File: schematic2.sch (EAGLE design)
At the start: 76 parts, among them IC6 DS3231/SO

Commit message: Corrected unity gain buffer amplifiers for reference voltages into the instrumentation amps.
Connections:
- new net REF_BEAM: BEAM_Z.REF, REFC.-IN, REFC.OUT
- new net REF_JOYX: JOY_Y.REF, REFB.-IN, REFB.OUT
- new net REF_JOYY: JOY_X.REF, REFA.-IN, REFA.OUT
- net A3: now also REFA.+IN; no longer JOY_X.REF, REFA.-IN, REFA.OUT
- net A4: now also REFB.+IN; no longer JOY_Y.REF, REFB.-IN, REFB.OUT
- net A5: now also REFC.+IN; no longer BEAM_Z.REF, REFC.-IN, REFC.OUT
- net AGND: no longer REFA.+IN, REFB.+IN, REFC.+IN

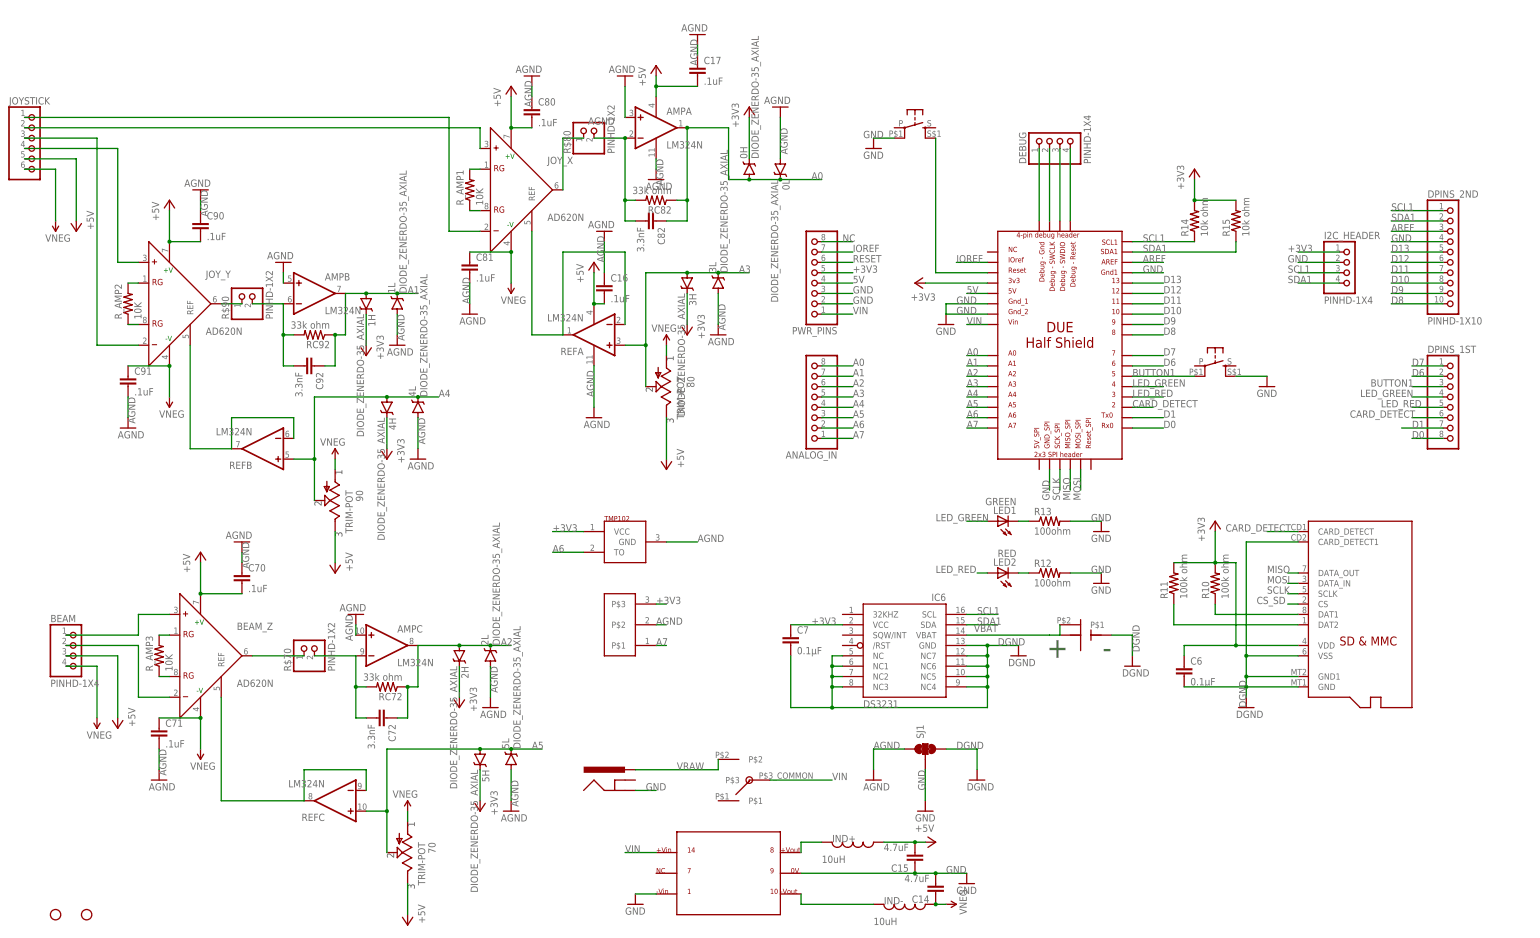
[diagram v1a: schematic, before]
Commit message: Moved the amps around again, wired most of the traces. Discovered that I never connected CS_SD, it is now wired to Due pin D10.
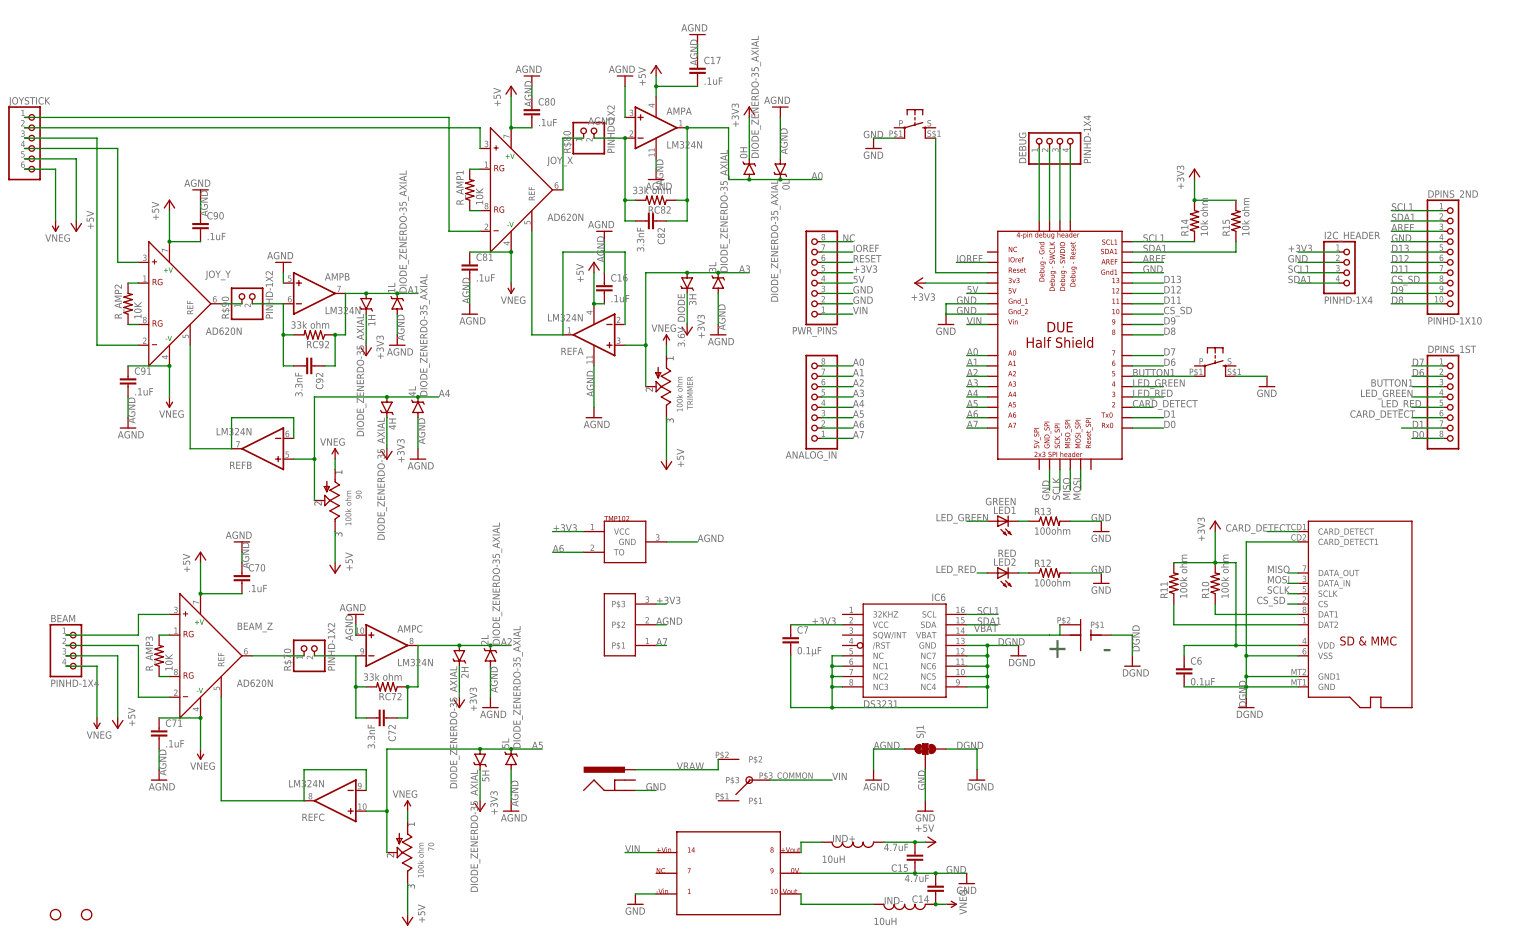
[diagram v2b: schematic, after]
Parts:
- removed 80: TRIM-POT, Felicia_force_logger:TRIM-POT
- added TRIMMER: 100k ohm, Felicia_force_logger:TRIMMER_POTENTIOMETER_TT_ELEC67W
- 3H: value DIODE_ZENERDO-35_AXIAL -> 3.6V_DIODE
- 70, 90: value TRIM-POT -> 100k ohm; device Felicia_force_logger:TRIM-POT -> miller:TRIMMER_POTENTIOMETER_TT_ELEC67W
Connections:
- removed net D10: DPINS_2ND.8, U$1.10
- net +5V: now also TRIMMER.P$3; no longer 80.P$3
- net A3: now also TRIMMER.P$2; no longer 80.P$2
- net CS_SD: now also DPINS_2ND.8, U$1.10
- net VNEG: now also TRIMMER.P$1; no longer 80.P$1
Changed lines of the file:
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@@
 <?xml version="1.0" encoding="utf-8"?>
 <!DOCTYPE eagle SYSTEM "eagle.dtd">
-<eagle version="7.0.0">
+<eagle version="7.2.0">
 <drawing>
 <settings>
@@
 <layer number="113" name="IDFDebug" color="4" fill="1" visible="yes" active="yes"/>
 <layer number="116" name="Patch_BOT" color="9" fill="4" visible="yes" active="yes"/>
+<layer number="118" name="Rect_Pads" color="7" fill="1" visible="no" active="no"/>
 <layer number="121" name="_tsilk" color="7" fill="1" visible="yes" active="yes"/>
 <layer number="122" name="_bsilk" color="7" fill="1" visible="yes" active="yes"/>
@@
 <layer number="223" name="223bmp" color="24" fill="1" visible="no" active="no"/>
 <layer number="224" name="224bmp" color="25" fill="1" visible="no" active="no"/>
+<layer number="231" name="Eagle3D_PG1" color="7" fill="1" visible="no" active="no"/>
+<layer number="232" name="Eagle3D_PG2" color="7" fill="1" visible="no" active="no"/>
+<layer number="233" name="Eagle3D_PG3" color="7" fill="1" visible="no" active="no"/>
 <layer number="248" name="Housing" color="7" fill="1" visible="yes" active="yes"/>
 <layer number="249" name="Edge" color="7" fill="1" visible="yes" active="yes"/>
@@
 <part name="BEAM_Z" library="Felicia_force_logger" deviceset="AD620" device="N"/>
 <part name="REF" library="Felicia_force_logger" deviceset="LM324" device="N"/>
-<part name="90" library="Felicia_force_logger" deviceset="TRIM-POT" device=""/>
-<part name="80" library="Felicia_force_logger" deviceset="TRIM-POT" device=""/>
-<part name="70" library="Felicia_force_logger" deviceset="TRIM-POT" device=""/>
+<part name="90" library="miller" deviceset="TRIMMER_POTENTIOMETER_TT_ELEC" device="67W" value="100k ohm"/>
+<part name="TRIMMER" library="Felicia_force_logger" deviceset="TRIMMER_POTENTIOMETER_TT_ELEC" device="67W" value="100k ohm"/>
+<part name="70" library="miller" deviceset="TRIMMER_POTENTIOMETER_TT_ELEC" device="67W" value="100k ohm"/>
 <part name="AMP" library="Felicia_force_logger" deviceset="LM324" device="N"/>
 <part name="GND4" library="Felicia_force_logger" deviceset="AGND" device=""/>
@@
 <part name="+3V4" library="supply1" deviceset="+3V3" device=""/>
 <part name="GND13" library="Felicia_force_logger" deviceset="AGND" device=""/>
-<part name="3H" library="Felicia_force_logger" deviceset="DIODE_ZENER" device="DO-35_AXIAL"/>
+<part name="3H" library="Felicia_force_logger" deviceset="DIODE_ZENER" device="DO-35_AXIAL" value="3.6V_DIODE"/>
 <part name="3L" library="Felicia_force_logger" deviceset="DIODE_ZENER" device="DO-35_AXIAL"/>
 <part name="+3V5" library="supply1" deviceset="+3V3" device=""/>
@@
 <instance part="REF" gate="C" x="73.66" y="33.02" rot="R180"/>
 <instance part="90" gate="G$1" x="73.66" y="106.68" rot="R270"/>
-<instance part="80" gate="G$1" x="154.94" y="134.62" rot="R270"/>
+<instance part="TRIMMER" gate="G$1" x="154.94" y="134.62" rot="R270"/>
 <instance part="70" gate="G$1" x="91.44" y="20.32" rot="R270"/>
 <instance part="AMP" gate="A" x="152.4" y="198.12"/>
@@
 </segment>
 <segment>
-<pinref part="80" gate="G$1" pin="P$2"/>
+<pinref part="TRIMMER" gate="G$1" pin="P$2"/>
 <pinref part="3L" gate="G$1" pin="C"/>
 <junction x="167.64" y="162.56"/>
@@
 </segment>
 <segment>
-<pinref part="80" gate="G$1" pin="P$3"/>
+<pinref part="TRIMMER" gate="G$1" pin="P$3"/>
 <pinref part="P+3" gate="1" pin="+5V"/>
 <wire x1="154.94" y1="116.84" x2="154.94" y2="127" width="0.1524" layer="91"/>
@@
 <label x="299.72" y="81.28" size="1.778" layer="95"/>
 </segment>
+<segment>
+<pinref part="U$1" gate="G$1" pin="10"/>
+<wire x1="269.24" y1="152.4" x2="276.86" y2="152.4" width="0.1524" layer="91"/>
+<label x="276.86" y="152.4" size="1.778" layer="95"/>
+</segment>
+<segment>
+<pinref part="DPINS_2ND" gate="G$1" pin="8"/>
+<wire x1="345.44" y1="160.02" x2="332.74" y2="160.02" width="0.1524" layer="91"/>
+<label x="332.74" y="160.02" size="1.778" layer="95"/>
+</segment>
 </net>
 <net name="GND" class="0">
@@
 </segment>
 </net>
-<net name="D10" class="0">
-<segment>
-<pinref part="U$1" gate="G$1" pin="10"/>
-<wire x1="269.24" y1="152.4" x2="276.86" y2="152.4" width="0.1524" layer="91"/>
-<label x="276.86" y="152.4" size="1.778" layer="95"/>
-</segment>
-<segment>
-<pinref part="DPINS_2ND" gate="G$1" pin="8"/>
-<wire x1="345.44" y1="160.02" x2="332.74" y2="160.02" width="0.1524" layer="91"/>
-<label x="332.74" y="160.02" size="1.778" layer="95"/>
-</segment>
-</net>
 <net name="D11" class="0">
 <segment>
@@
 </segment>
 <segment>
-<pinref part="80" gate="G$1" pin="P$1"/>
+<pinref part="TRIMMER" gate="G$1" pin="P$1"/>
 <pinref part="P-1" gate="G$2" pin="VNEG"/>
 <wire x1="154.94" y1="144.78" x2="154.94" y2="142.24" width="0.1524" layer="91"/>

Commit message: Swapped out I2C header with a 6 pin version that could work with Adafruit I2C OLED display. Moved Reset button to upper corner like the Due's location. Moved LEDs closer to their associated digital pins. Finished wiring the analog and digital sections. Need to deal with ground planes on bottom still.
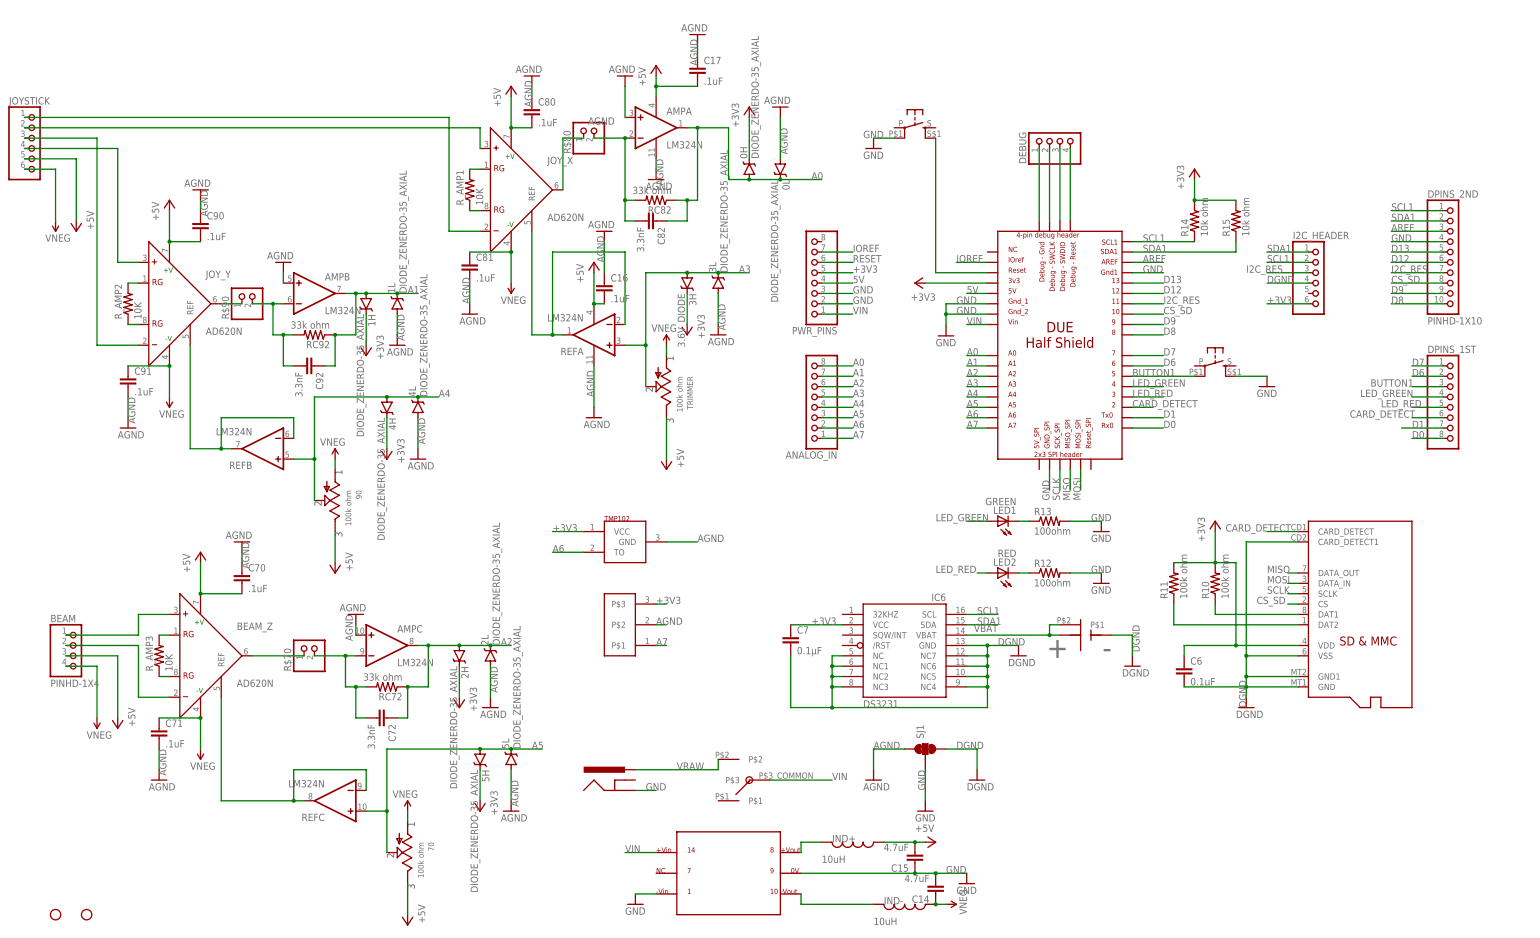
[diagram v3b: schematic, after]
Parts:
- ANALOG7_HEADER: value PINHD-1X3 -> (none)
- BEAM: device Felicia_force_logger:PINHD-1X4 -> Felicia_force_logger:PINHD-1X4LOCK
- DEBUG: value PINHD-1X4 -> (none); device Felicia_force_logger:PINHD-1X4 -> Felicia_force_logger:PINHD-1X4LOCK
- I2C_HEADER: value PINHD-1X4 -> (none); device Felicia_force_logger:PINHD-1X4 -> Felicia_force_logger:PINHD-1X6LOCK
- JOYSTICK: device Felicia_force_logger:PINHD-1X6 -> Felicia_force_logger:PINHD-1X6LOCK
- R$70, R$80, R$90: value PINHD-1X2 -> (none)
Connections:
- removed net D11: DPINS_2ND.7, U$1.11
- removed net NC: PWR_PINS.8
- new net I2C_RES: DPINS_2ND.7, I2C_HEADER.3, U$1.11
- net +3V3: now also I2C_HEADER.6; no longer I2C_HEADER.1
- net DGND: now also I2C_HEADER.4
- net GND: no longer I2C_HEADER.2
- net SCL1: now also I2C_HEADER.2; no longer I2C_HEADER.3
- net SDA1: now also I2C_HEADER.1; no longer I2C_HEADER.4
